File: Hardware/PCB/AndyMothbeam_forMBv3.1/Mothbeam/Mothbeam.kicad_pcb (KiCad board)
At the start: 2 copper layers, 22 x 45 mm, 24 parts, among them CN1 X6511FRS-04-C85D30, SW2 SW_DIP_x04, U1 BCR421U, U2 BCR421U, U3 BCR421U

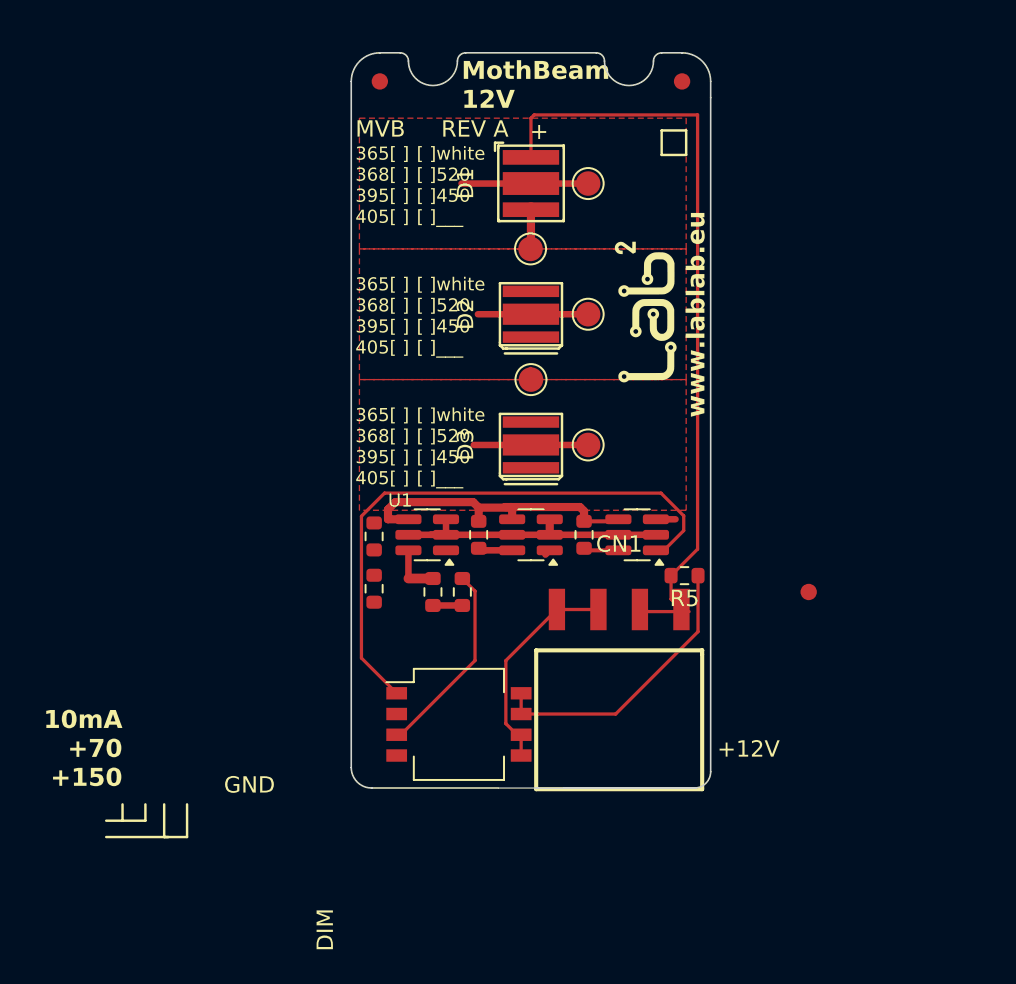
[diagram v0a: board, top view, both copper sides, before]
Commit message: mothbeam routes all cables
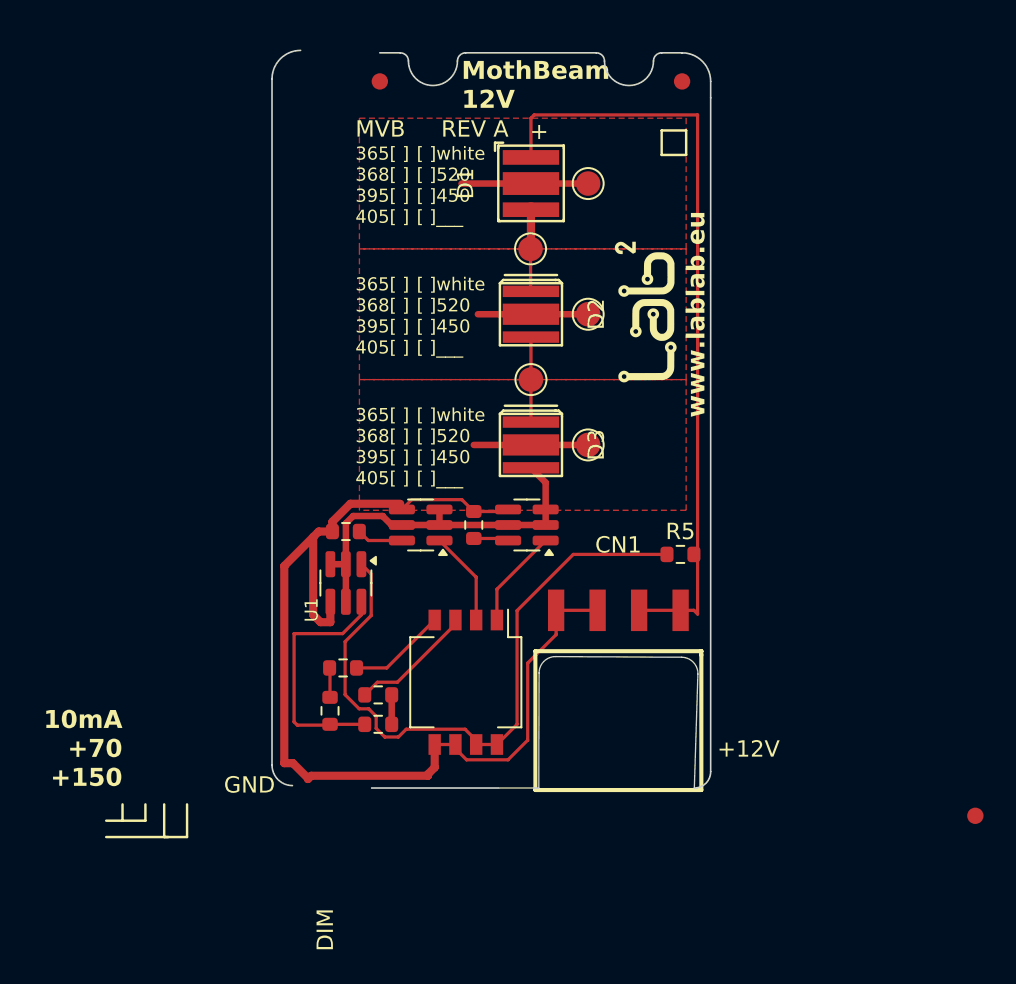
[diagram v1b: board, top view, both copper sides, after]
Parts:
- moved FID1 17.1 mm to (142.2, 76.7)
- moved R3 11.0 mm to (102.7, 70.3), turned to 90 degrees
- moved R2 8.77 mm to (105.7, 71.1), turned to 0 degrees
- moved R6 8.14 mm to (105.7, 69.3), turned to 180 degrees
- moved R9 8.13 mm to (103.7, 59.3), turned to 180 degrees
- moved R1 6.78 mm to (111.5, 58.9)
- moved U2 6.78 mm to (108.2, 58.9)
- moved U3 6.78 mm to (114.8, 58.9)
- moved U1 5.79 mm to (103.7, 62.5), turned to -90 degrees
- moved R4 5.21 mm to (103.5, 67.7), turned to 0 degrees
- moved SW2 2.61 mm to (111.0, 68.5), turned to -90 degrees
- moved R5 1.32 mm to (124.2, 60.7), turned to 180 degrees
- moved CN1 0.07 mm to (120.3, 64.1)
- turned D2 to -90 degrees
- turned D3 to -90 degrees
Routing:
- net GND: track 32.0 -> 64.5 mm
- net Net-(U3-EN): track 35.7 -> 6.10 mm
- net EN: track 17.6 -> 39.7 mm
- net Net-(U1-REXT): track 3.22 -> 15.2 mm
- net Net-(R4-Pad2): track 0.00 -> 6.00 mm
- net Net-(U2-EN): track 0.37 -> 5.80 mm
- net Net-(D2-K): track 0.16 -> 5.36 mm
- net Net-(R6-Pad2): track 12.0 -> 7.60 mm
- net /LED-: track 19.2 -> 23.2 mm
- net Net-(D1-K): track 2.59 -> 5.16 mm
- net Net-(R3-Pad2): track 0.00 -> 1.81 mm
- net Net-(U2-REXT): track 1.90 -> 2.83 mm
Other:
- board size 22 x 45 mm -> 26.8 x 45.1 mm

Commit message: Mothbeam Looking good! ready for review!
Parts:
- moved H1 5.41 mm to (121.7, 51.4)
- moved D1 2.25 mm to (112.8, 38.0)
- moved D2 2.25 mm to (112.8, 46.0)
- moved D3 2.25 mm to (112.8, 54.0)
- moved TP1 2.25 mm to (112.8, 50.0)
- moved TP2 2.25 mm to (116.2, 38.0)
- moved TP3 2.25 mm to (112.7, 42.0)
- moved TP4 2.25 mm to (116.2, 46.0)
- moved TP5 2.25 mm to (116.2, 54.0)
- moved R9 1.55 mm to (103.7, 60.9)
- moved R1 1.55 mm to (111.5, 60.5)
- moved U2 1.55 mm to (108.3, 60.5)
- moved U3 1.55 mm to (114.8, 60.5)
- moved U1 1.55 mm to (103.7, 64.0)
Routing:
- net Net-(U1-REXT): track 15.2 -> 10.7 mm
- net GND: track 64.5 -> 61.1 mm
- net /LED-: track 23.2 -> 25.8 mm
- net /LED+: track 46.9 -> 49.1 mm
- net Net-(U3-EN): track 6.10 -> 4.39 mm
- net Net-(U2-EN): track 5.80 -> 4.21 mm
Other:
- board size 26.8 x 45.1 mm -> 26.8 x 45 mm
- board text added: "+150mA"
- board text added: "+70mA"
- board text added: "Current = 10ma"
- board text added: "Modified by: Digital Naturalism Labs for Mothbox"
- board text added: "MothBeam 12V v5.0.0"
- board text added: "Originally By:"
- board text removed: "10mA +70 +150"
- board text removed: "DIM"
- board text removed: "MothBeam 12V"

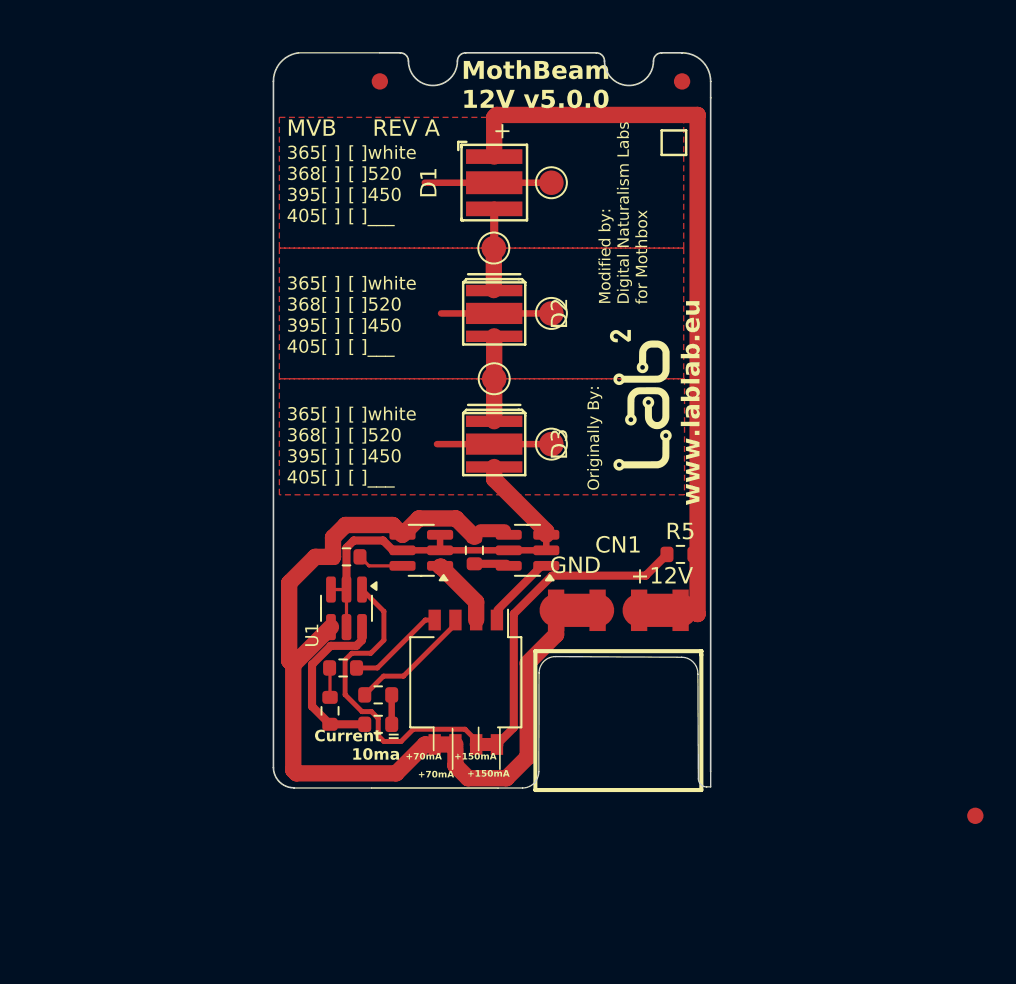
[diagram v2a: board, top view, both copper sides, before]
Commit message: no DRC errors on Mothbeam!
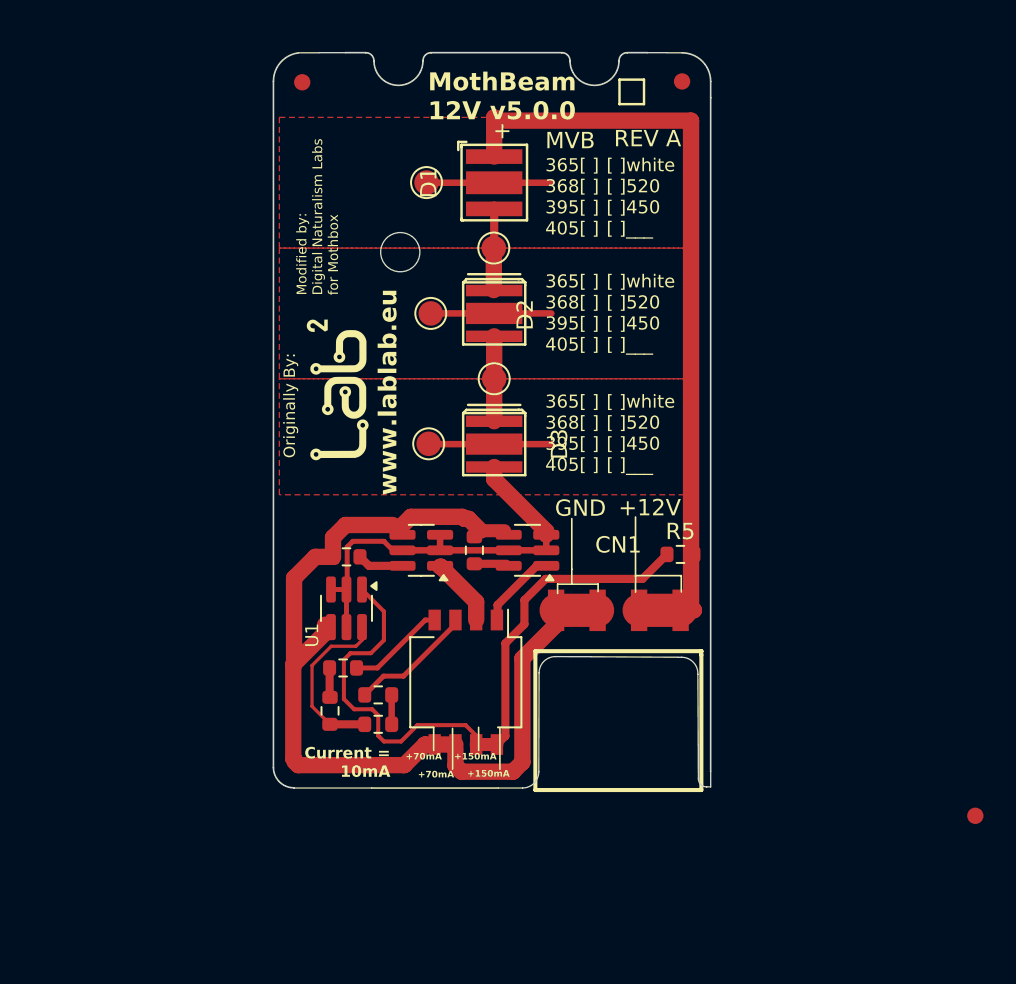
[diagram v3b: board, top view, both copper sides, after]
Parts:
- moved H1 18.6 mm to (103.1, 50.8)
- moved TP2 7.64 mm to (108.6, 37.9)
- moved TP5 7.51 mm to (108.7, 53.9)
- moved TP4 7.38 mm to (108.9, 46.0)
- moved FID2 4.75 mm to (101.0, 31.8)
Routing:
- net GND: track 61.1 -> 58.0 mm
- net /LED+: track 49.1 -> 47.9 mm
- net EN: track 39.9 -> 40.8 mm
- net /LED-: track 25.8 -> 25.2 mm
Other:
- outline, holes or cut-outs redrawn
- board text added: "Current = 10mA"
- board text removed: "Current = 10ma"

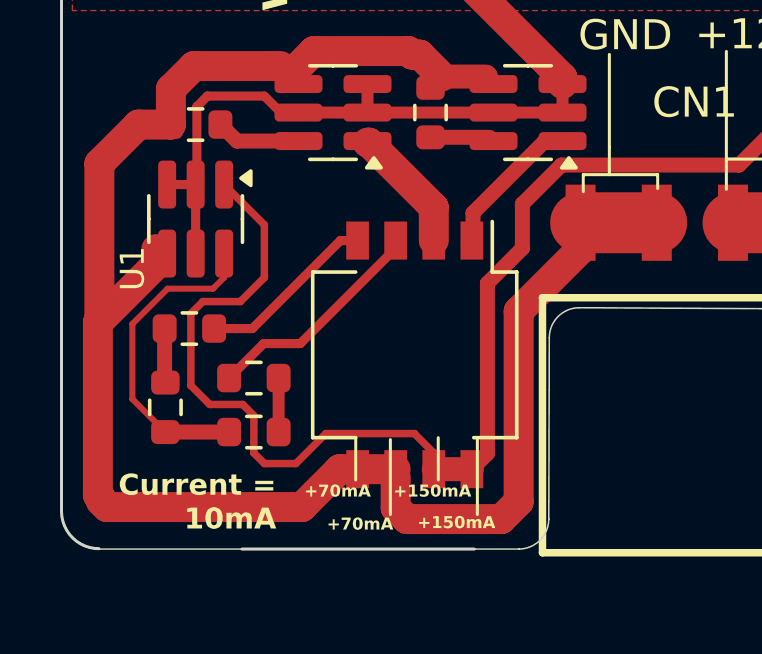
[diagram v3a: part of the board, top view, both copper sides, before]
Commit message: widen tiny bit track
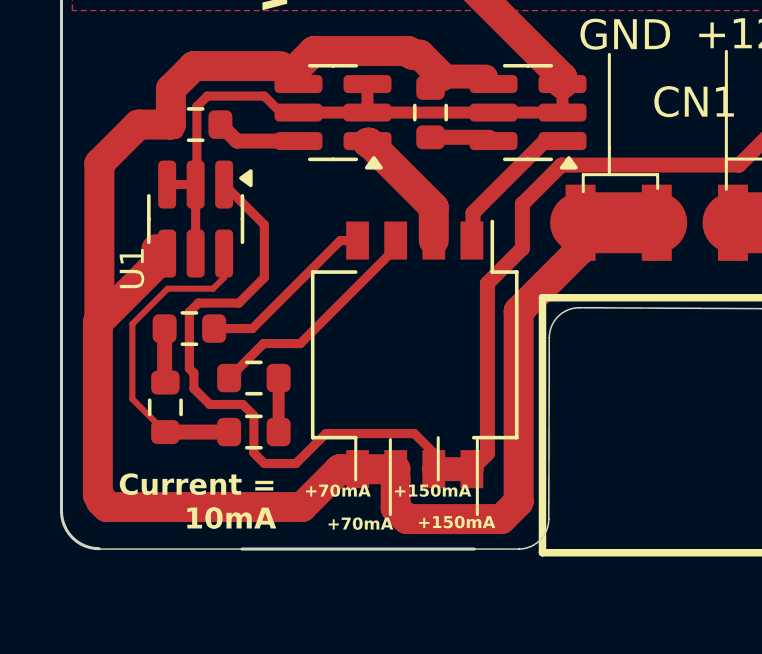
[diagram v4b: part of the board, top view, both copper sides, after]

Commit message: all LCSC parts except resistors!
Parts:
- removed FID1, FID2, FID3: Fiducial, Fiducial:Fiducial_1mm_Mask3mm
- added REF**: MountingHole_2.2mm_M2_DIN965_Pad, MountingHole:MountingHole_2.2mm_M2_DIN965_Pad, F.Cu at (102.1, 32.7)
- added REF**: MountingHole_2.2mm_M2_DIN965_Pad, MountingHole:MountingHole_2.2mm_M2_DIN965_Pad, F.Cu at (123.3, 32.6)
- D1: footprint easyeda2kicad:LED-SMD_3P-L3.5-W3.5_M3535O1IRS13G06 -> easyeda2kicad:LED-SMD_3P-L3.5-W3.5-R-RD-C
- SW2: footprint Button_Switch_SMD:SW_DIP_SPSTx04_Slide_KingTek_DSHP04TS_W7.62mm_P1.27mm -> easyeda2kicad:SW-SMD_8P-L6.7-W5.4-P1.27-LS8.5
- U1, U2, U3: footprint Package_TO_SOT_SMD:SC-74-6_1.55x2.9mm_P0.95mm -> easyeda2kicad:SOT-23-6_L2.9-W1.6-P0.95-LS2.8-BL
- turned D2 to 90 degrees
- turned D3 to 90 degrees
- turned SW2 to 180 degrees
- turned U1 to 180 degrees
- turned U2 to 90 degrees
- turned U3 to 90 degrees
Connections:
- D1 pad 1: Net-(D1-K) -> /LED+
- D1 pad 2: /LED+ -> Net-(D1--)
- D2 pad 1: Net-(D2-K) -> Net-(D1--)
- D2 pad 2: Net-(D1-K) -> Net-(D2-A)
- D3 pad 1: /LED- -> Net-(D2-A)
- D3 pad 2: Net-(D2-K) -> /LED-
- R2 pad 1: Net-(U1-REXT) -> /LED-
- R3 pad 1: Net-(U1-REXT) -> /LED-
- TP1 pad 1: Net-(D2-K) -> Net-(D2-A)
- TP3 pad 1: Net-(D1-K) -> Net-(D1--)
- U1 pad 6: Net-(U1-REXT) -> /LED-
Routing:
- net /LED-: track 25.2 -> 37.4 mm
- net Net-(U1-REXT): track 10.7 -> 0.00 mm
- net Net-(D2-K): track 5.36 -> 0.00 mm
- net Net-(D2-A): track 0.00 -> 5.36 mm
- net Net-(D1-K): track 5.16 -> 0.00 mm
- net Net-(D1--): track 0.00 -> 5.16 mm
- net /LED+: track 47.9 -> 44.3 mm
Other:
- outline, holes or cut-outs redrawn
- board text added: "MothBeam 12V v5.0.1"
- board text removed: "MothBeam 12V v5.0.0"
